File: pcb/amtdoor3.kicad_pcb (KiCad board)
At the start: 2 copper layers, 65 x 30 mm, 45 parts, among them P1 CONN_01X03, P2 dnp-REF-182665-01, P3 CONN_01X03, P4 CONN_01X04, P5 CONN_01X02, P6 CONN_01X02, Q1 Q_NMOS_GSD, Q2 Q_PMOS_HP, Q3 DMMT3906_Dual_PNP, Q4 Q_NMOS_GSD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

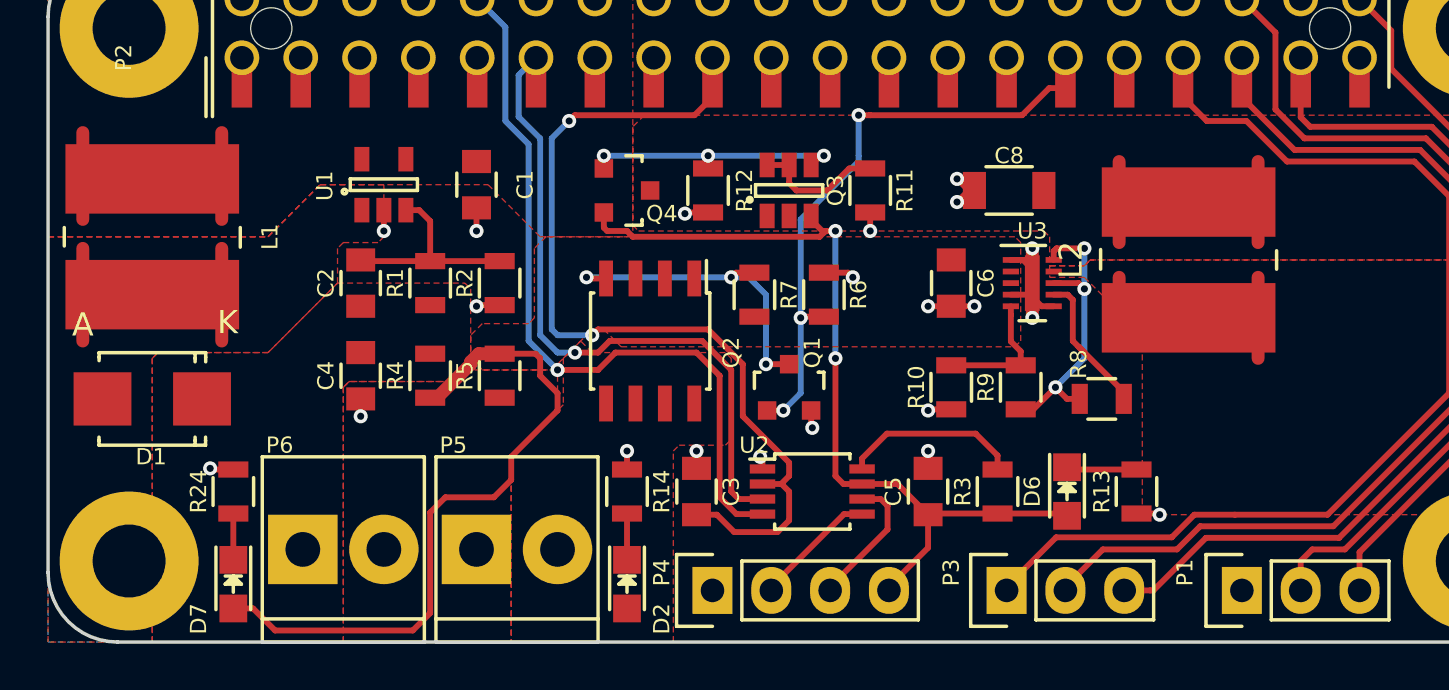
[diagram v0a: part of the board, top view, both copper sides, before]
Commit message: clean up silkscreen, set soldermask expansion, write gerbers
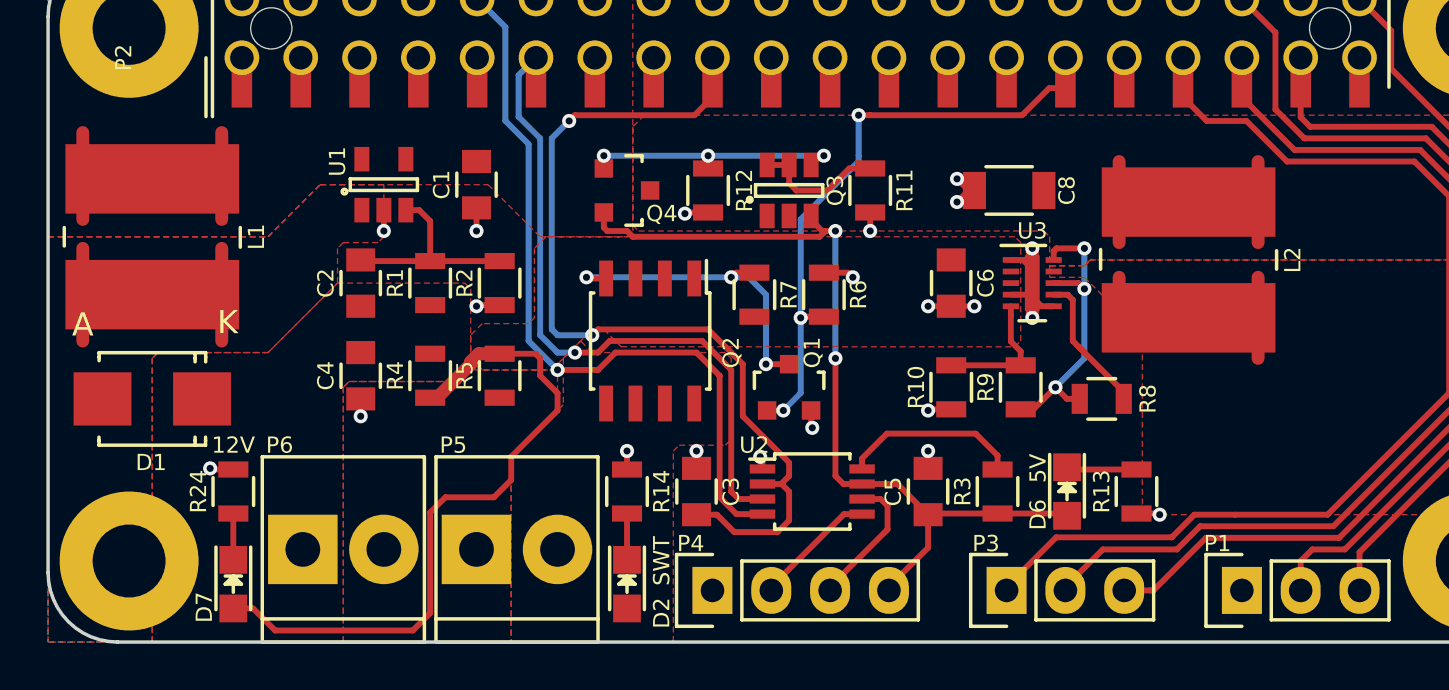
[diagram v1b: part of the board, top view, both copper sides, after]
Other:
- rule pad_to_mask_clearance: 0.2 -> 0.051
- board text added: "12V"
- board text added: "5V"
- board text added: "SWT"
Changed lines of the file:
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@@
     (links 142)
     (no_connects 0)
-    (area 97.2318 83.759999 167.261533 132.2682)
+    (area 97.2318 97.3318 167.261533 132.2682)
     (thickness 1.6)
-    (drawings 16)
+    (drawings 11)
     (tracks 389)
     (zones 0)
@@
     (pad_size 1.524 1.524)
     (pad_drill 0.762)
-    (pad_to_mask_clearance 0.2)
+    (pad_to_mask_clearance 0.051)
+    (solder_mask_min_width 0.077)
     (aux_axis_origin 0 0)
     (visible_elements FFFFFF7F)
     (pcbplotparams
-      (layerselection 0x00030_80000001)
-      (usegerberextensions false)
+      (layerselection 0x010fc_80000001)
+      (usegerberextensions true)
       (excludeedgelayer true)
       (linewidth 0.100000)
@@
       (viasonmask false)
       (mode 1)
-      (useauxorigin false)
+      (useauxorigin true)
       (hpglpennumber 1)
       (hpglpenspeed 20)
@@
       (outputformat 1)
       (mirror false)
-      (drillshape 1)
+      (drillshape 0)
       (scaleselection 1)
-      (outputdirectory ""))
+      (outputdirectory gerber/))
   )
   (net 0 "")
@@
     (tags "Diode SMB Standard")
     (attr smd)
-    (fp_text reference D1 (at 0.05 -2.5 180) (layer F.SilkS)
+    (fp_text reference D1 (at 0.05 -2.75 180) (layer F.SilkS)
       (effects (font (size 0.7 0.7) (thickness 0.15)))
     )
@@
     (tags "Choke, Drossel, WE-PD2, Typ L, Wuerth, SMD,")
     (attr smd)
-    (fp_text reference L1 (at 0 -5.08 270) (layer F.SilkS)
+    (fp_text reference L1 (at 0 -4.5 270) (layer F.SilkS)
       (effects (font (size 0.7 0.7) (thickness 0.15)))
     )
@@
     (descr "Through hole socket strip")
     (tags "socket strip")
-    (fp_text reference P1 (at -2.46 -0.77 90) (layer F.SilkS)
+    (fp_text reference P1 (at -1.05 -2.02 180) (layer F.SilkS)
       (effects (font (size 0.7 0.7) (thickness 0.15)))
     )
@@
     (descr "Through hole socket strip")
     (tags "socket strip")
-    (fp_text reference P3 (at -2.39 -0.77 90) (layer F.SilkS)
+    (fp_text reference P3 (at -0.89 -2.02 180) (layer F.SilkS)
       (effects (font (size 0.7 0.7) (thickness 0.15)))
     )
@@
     (tags SOT-23-5)
     (attr smd)
-    (fp_text reference U1 (at -0.05 -2.55 90) (layer F.SilkS)
+    (fp_text reference U1 (at 1 -2 90) (layer F.SilkS)
       (effects (font (size 0.7 0.7) (thickness 0.15)))
     )
@@
     (tags "capacitor 0805")
     (attr smd)
-    (fp_text reference C1 (at 0 -2.1 270) (layer F.SilkS)
+    (fp_text reference C1 (at 0 1.5 270) (layer F.SilkS)
       (effects (font (size 0.7 0.7) (thickness 0.15)))
     )
@@
     (tags "LED 0805 SMD")
     (attr smd)
-    (fp_text reference D6 (at 0 1.5 270) (layer F.SilkS)
+    (fp_text reference D6 (at 1 1.25 270) (layer F.SilkS)
       (effects (font (size 0.7 0.7) (thickness 0.15)))
     )
@@
     (tags "LED 0805 SMD")
     (attr smd)
-    (fp_text reference D7 (at 1.5 1.5 270) (layer F.SilkS)
+    (fp_text reference D7 (at 1 1.25 450) (layer F.SilkS)
       (effects (font (size 0.7 0.7) (thickness 0.15)))
     )
@@
     (descr "Through hole socket strip")
     (tags "socket strip")
-    (fp_text reference P4 (at -2.19 -0.77 90) (layer F.SilkS)
+    (fp_text reference P4 (at -0.94 -2.02 180) (layer F.SilkS)
       (effects (font (size 0.7 0.7) (thickness 0.15)))
     )
@@
     (tags "capacitor 1206")
     (attr smd)
-    (fp_text reference C8 (at 0 1.5 180) (layer F.SilkS)
+    (fp_text reference C8 (at -2.5 0 270) (layer F.SilkS)
       (effects (font (size 0.7 0.7) (thickness 0.15)))
     )
@@
     (tags "LED 0805 SMD")
     (attr smd)
-    (fp_text reference D2 (at 1.5 -1.5 270) (layer F.SilkS)
+    (fp_text reference D2 (at 1.25 -1.5 270) (layer F.SilkS)
       (effects (font (size 0.7 0.7) (thickness 0.15)))
     )
@@
     (tags "resistor 0805")
     (attr smd)
-    (fp_text reference R8 (at -1 -1.5 90) (layer F.SilkS)
+    (fp_text reference R8 (at 2 0 90) (layer F.SilkS)
       (effects (font (size 0.7 0.7) (thickness 0.15)))
     )
@@
     (tags "Choke, Drossel, WE-PD2, Typ L, Wuerth, SMD,")
     (attr smd)
-    (fp_text reference L2 (at 0 -5.08 90) (layer F.SilkS)
-      (effects (font (size 1 1) (thickness 0.15)))
+    (fp_text reference L2 (at 0 4.5 90) (layer F.SilkS)
+      (effects (font (size 0.7 0.7) (thickness 0.15)))
     )
     (fp_text value 10uH (at 0 6.35 90) (layer F.Fab)
-      (effects (font (size 1 1) (thickness 0.15)))
+      (effects (font (size 0.7 0.7) (thickness 0.15)))
     )
     (fp_line (start -0.39878 3.79984) (end 0.39878 3.79984) (layer F.SilkS) (width 0.15))
@@
       (net 47 /VOS_5V))
   )
-  (gr_line (start 160.06 96.56) (end 142.28 96.56) (layer F.CrtYd) (width 0.2))
-  (gr_line (start 160.06 83.86) (end 160.06 96.56) (layer F.CrtYd) (width 0.2))
-  (gr_line (start 142.28 83.86) (end 160.06 83.86) (layer F.CrtYd) (width 0.2))
-  (gr_line (start 142.28 96.56) (end 142.28 83.86) (layer F.CrtYd) (width 0.2))
-  (gr_line (start 138.24 84.4) (end 138.24 94.56) (layer F.CrtYd) (width 0.2))
-  (gr_line (start 125.54 84.4) (end 138.24 84.4) (layer F.CrtYd) (width 0.2))
-  (gr_line (start 125.54 94.56) (end 125.54 84.4) (layer F.CrtYd) (width 0.2))
-  (gr_line (start 138.24 94.56) (end 125.54 94.56) (layer F.CrtYd) (width 0.2))
+  (gr_text 12V (at 108 121.5) (layer F.SilkS)
+    (effects (font (size 0.7 0.7) (thickness 0.15)))
+  )
+  (gr_text SWT (at 126.5 126.5 90) (layer F.SilkS)
+    (effects (font (size 0.7 0.7) (thickness 0.15)))
+  )
+  (gr_text 5V (at 142.75 122.5 90) (layer F.SilkS)
+    (effects (font (size 0.7 0.7) (thickness 0.15)))
+  )
   (gr_arc (start 162 127) (end 165 127) (angle 90) (layer Edge.Cuts) (width 0.15))
   (gr_arc (start 162 103) (end 162 100) (angle 90) (layer Edge.Cuts) (width 0.15))

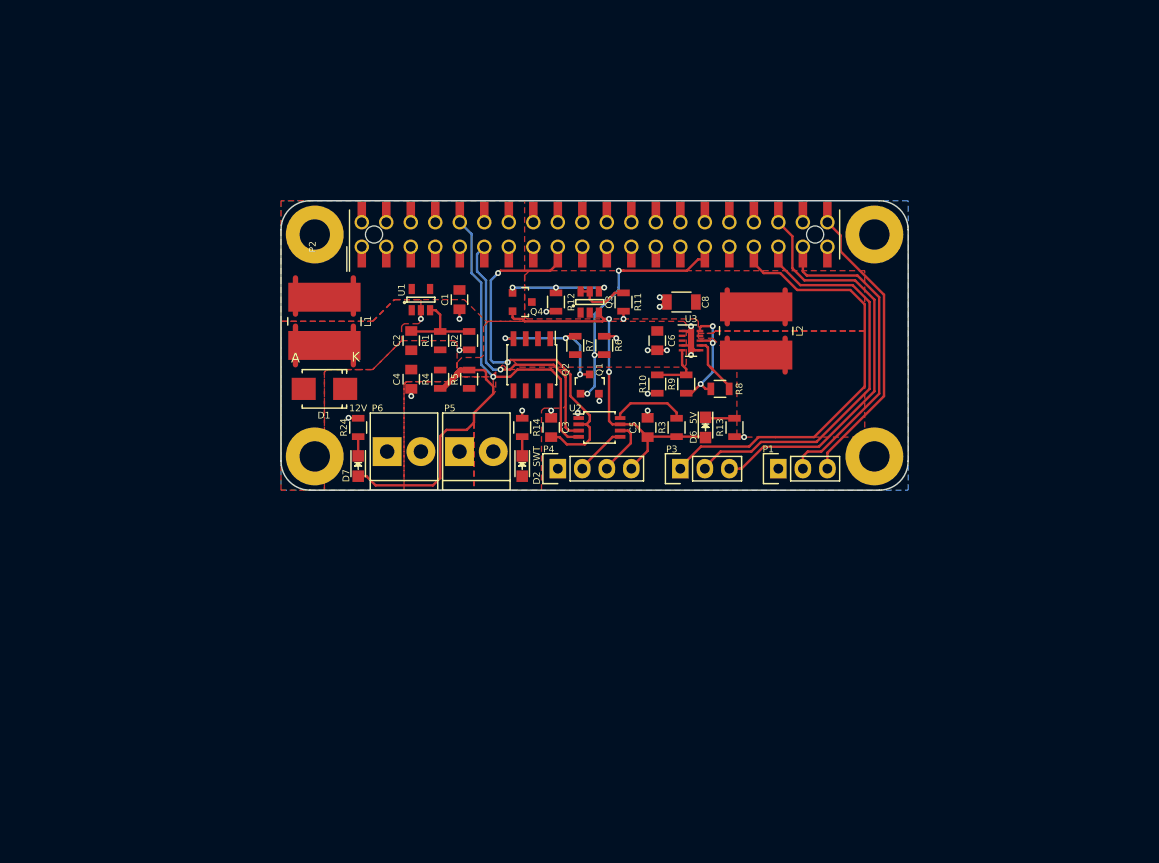
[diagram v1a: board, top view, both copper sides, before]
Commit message: new rev schematic updates and footprint grouping
* change level shifter to NFET gates w/ pull up b/c NVT2002 leaks 5V EN to 3.3V rail
* add selectable, fused output voltage to each port
* rename P2 to P4 so the output ports are P1, P2, P3
* use level shifting on all ports
* reassign GPIO to ports so we have UART TX+RX, PWM, and plain GPIO
* add fuses and DNPs so boost and buck can be populated but not interfere
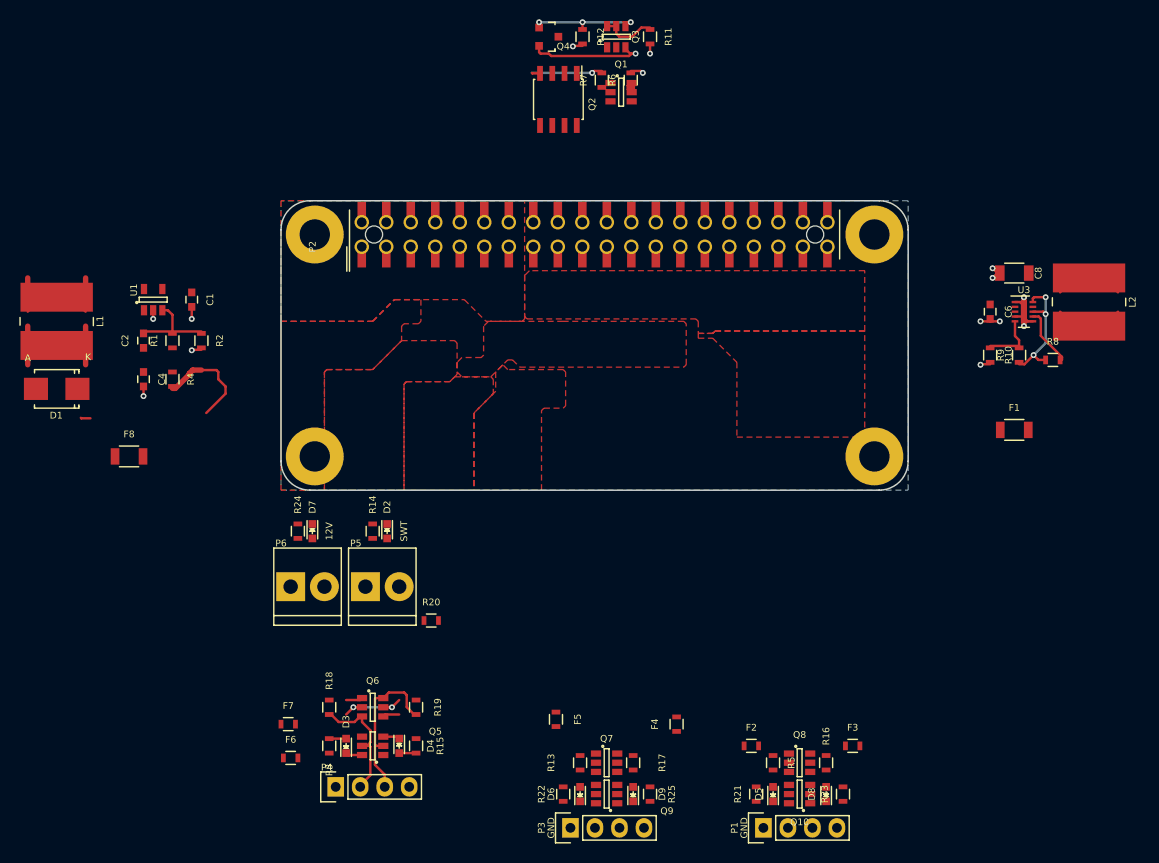
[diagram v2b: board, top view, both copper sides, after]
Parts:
- removed C3, C5: 0.1uF, Capacitors_SMD:C_0805
- removed U2: NVT2002, Housings_SSOP:TSSOP-8_3x3mm_Pitch0.65mm
- added D3: LED Green, LEDs:LED_0603, F.Cu at (106.8, 156.5)
- added D4: LED Green, LEDs:LED_0603, F.Cu at (112.2, 156.5)
- added D5: LED Green, LEDs:LED_0603, F.Cu at (151.0, 161.5)
- added D8: LED Green, LEDs:LED_0603, F.Cu at (156.5, 161.5)
- added D9: LED Green, LEDs:LED_0603, F.Cu at (136.5, 161.5)
- added F1: 250mA, Resistors_SMD:R_1206, F.Cu at (176.0, 123.8)
- added F2: F_Small, Resistors_SMD:R_0603, F.Cu at (148.8, 156.5)
- added F3: F_Small, Resistors_SMD:R_0603, F.Cu at (159.2, 156.5)
- added F4: F_Small, Resistors_SMD:R_0603, F.Cu at (141.0, 154.2)
- added F5: F_Small, Resistors_SMD:R_0603, F.Cu at (128.5, 153.8)
- added F6: F_Small, Resistors_SMD:R_0603, F.Cu at (101.0, 157.8)
- added F7: F_Small, Resistors_SMD:R_0603, F.Cu at (100.8, 154.2)
- added F8: 500mA, Resistors_SMD:R_1206, F.Cu at (84.2, 126.5)
- added Q10: Q_NMOS_DUAL, TO_SOT_Packages_SMD:SOT-23-6, F.Cu at (153.8, 161.5)
- added Q5: Q_NMOS_DUAL, TO_SOT_Packages_SMD:SOT-23-6, F.Cu at (109.5, 156.5)
- added Q6: Q_NMOS_DUAL, TO_SOT_Packages_SMD:SOT-23-6, F.Cu at (109.5, 152.5)
- added Q7: Q_NMOS_DUAL, TO_SOT_Packages_SMD:SOT-23-6, F.Cu at (133.8, 158.2)
- added Q8: Q_NMOS_DUAL, TO_SOT_Packages_SMD:SOT-23-6, F.Cu at (153.8, 158.2)
- added Q9: Q_NMOS_DUAL, TO_SOT_Packages_SMD:SOT-23-6, F.Cu at (133.8, 161.5)
- added R15: 1k, Resistors_SMD:R_0603, F.Cu at (114.0, 156.5)
- added R16: 10k, Resistors_SMD:R_0603, F.Cu at (156.5, 158.2)
- added R17: 10k, Resistors_SMD:R_0603, F.Cu at (136.5, 158.2)
- added R18: 10k, Resistors_SMD:R_0603, F.Cu at (105.0, 152.5)
- added R19: 10k, Resistors_SMD:R_0603, F.Cu at (114.0, 152.5)
- added R20: 10k, Resistors_SMD:R_0603, F.Cu at (115.6, 143.5)
- added R21: 1k, Resistors_SMD:R_0603, F.Cu at (149.2, 161.5)
- added R22: 1k, Resistors_SMD:R_0603, F.Cu at (129.2, 161.5)
- added R23: 1k, Resistors_SMD:R_0603, F.Cu at (158.2, 161.5)
- added R25: 1k, Resistors_SMD:R_0603, F.Cu at (138.2, 161.5)
- C1, C2, C6: footprint Capacitors_SMD:C_0805 -> Capacitors_SMD:C_0603
- C4: value 4.7uF -> 4.7uF 25V; footprint Capacitors_SMD:C_0805 -> Capacitors_SMD:C_0603
- C8: value 22uF -> 22uF 10V
- D1: value 10BQ015 -> 15V 1A
- D2, D6, D7: footprint LEDs:LED_0805 -> LEDs:LED_0603
- P1, P3: value CONN_01X03 -> CONN_01X04; footprint Socket_Strips:Socket_Strip_Straight_1x03 -> Socket_Strips:Socket_Strip_Straight_1x04
- Q1: value Q_NMOS_GSD -> Q_NMOS_DUAL; footprint TO_SOT_Packages_SMD:SOT-23 -> TO_SOT_Packages_SMD:SOT-23-6
- Q4: value Q_NMOS_GSD -> Q_PMOS_GSD
- R1, R10, R11, R12, R14, R2, R24, R4, R6, R7, R8, R9: footprint Resistors_SMD:R_0805 -> Resistors_SMD:R_0603
- R13: value 1k -> 10k; footprint Resistors_SMD:R_0805 -> Resistors_SMD:R_0603
- R3: value 10k -> 1k; footprint Resistors_SMD:R_0805 -> Resistors_SMD:R_0603
- R5: value dnp -> 10k; footprint Resistors_SMD:R_0805 -> Resistors_SMD:R_0603
- moved R5 50.7 mm to (151.0, 158.2)
- moved R3 48.8 mm to (105.0, 156.5)
- moved P4 40.2 mm to (105.7, 160.8)
- moved D6 40.2 mm to (131.0, 161.5), turned to 90 degrees
- moved P3 38.9 mm to (130.0, 165.0)
- moved R13 38.3 mm to (131.0, 158.2)
- moved P1 37.3 mm to (150.0, 165.0)
- moved C6 34.6 mm to (173.5, 111.5)
- moved C8 34.6 mm to (176.0, 107.5)
- moved L2 34.6 mm to (183.8, 110.5)
- moved R10 34.6 mm to (173.5, 116.0)
- moved R8 34.6 mm to (180.0, 116.5)
- moved R9 34.6 mm to (176.5, 116.0)
- moved U3 34.6 mm to (177.0, 111.5)
- moved Q1 30.4 mm to (135.2, 88.8)
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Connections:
- net /FB_12V renamed /BST_FB
- net /SW_12V renamed /BST_SW
- net /VSWITCHED_T renamed /P12V_SW
- C1 pad 1: +5V -> /P5V_BST
- C2 pad 1: +12V -> Net-(C2-Pad1)
- C4 pad 1: +12V -> Net-(C2-Pad1)
- C6 pad 1: /VSWITCHED -> Net-(C6-Pad1)
- D1 pad 1: +12V -> Net-(C2-Pad1)
- D6 pad 2: +5V -> Net-(D6-Pad2)
- D7 pad 2: /VSWITCHED -> +12V
- H1 pad 1: Net-(H1-Pad1) -> (no net)
- H2 pad 1: Net-(H2-Pad1) -> (no net)
- H3 pad 1: Net-(H3-Pad1) -> (no net)
- H4 pad 1: Net-(H4-Pad1) -> (no net)
- L1 pad 1: +5V -> /P5V_BST
- P1 pad 1: /GPIO20 -> GND
- P1 pad 2: /GPIO26 -> /PORT3-1
- P1 pad 3: /GPIO21_SCLK -> /PORT3-2
- P2 pad 17: +3V3 -> /RPI_3V3_2
- P3 pad 1: /GPIO13 -> GND
- P3 pad 2: /GPIO19 -> /PORT2-1
- P3 pad 3: /GPIO16_CE2# -> /PORT2-2
- P4 pad 4: +5V -> /VPORT1
- P6 pad 2: /VAUX -> +12V
- Q1 pad 1: /GPIO5 -> GND
- Q1 pad 2: GND -> /GPIO5
- Q1 pad 3: /VSW_D -> /GPIO22
- Q2 pad 1: /VSWITCHED -> +12V
- Q2 pad 2: /VSWITCHED -> +12V
- Q2 pad 3: /VSWITCHED -> +12V
- Q2 pad 4: /VSW_D -> /SW_D
- R1 pad 1: +12V -> Net-(C2-Pad1)
- R13 pad 1: Net-(D6-Pad1) -> /VPORT2
- R13 pad 2: GND -> /PORT2-1
- R3 pad 1: +5V -> /VPORT1
- R4 pad 1: +12V -> /P5V_BST
- R4 pad 2: /VSWITCHED -> +5V
- R5 pad 1: /VSWITCHED -> /VPORT3
- R5 pad 2: /VAUX -> /PORT3-1
- R7 pad 1: /VSWITCHED -> +12V
- R7 pad 2: /VSW_D -> /SW_D
- U1 pad 4: +5V -> /P5V_BST
- U1 pad 5: +5V -> /P5V_BST
- U3 pad 2: /VSWITCHED -> Net-(C6-Pad1)
- U3 pad 3: /VSWITCHED -> Net-(C6-Pad1)
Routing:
- net /GPIO13: track 46.2 -> 1.71 mm
- net /GPIO16_CE2#: track 44.4 -> 1.31 mm
- net /GPIO19: track 42.4 -> 1.71 mm
- net +3V3: track 39.9 -> 0.00 mm, vias 2 -> 0
- net +5V: track 56.3 -> 17.4 mm, vias 2 -> 1
- net /GPIO26: track 33.5 -> 1.31 mm
- net /GPIO15_RXD0: track 33.9 -> 3.04 mm, vias 1 -> 0
- net /GPIO21_SCLK: track 31.7 -> 1.31 mm
- net /VSWITCHED: track 29.7 -> 0.00 mm
- net /GPIO17: track 30.0 -> 1.31 mm, vias 1 -> 0
- net /GPIO5: track 26.5 -> 1.31 mm, vias 3 -> 0
- net /P5V_BST: track 0.00 -> 15.5 mm
- net /VSW_D: track 14.0 -> 0.00 mm, vias 3 -> 0
- net /RFID_EN: track 5.90 -> 16.7 mm
- net /VPORT3: track 0.00 -> 9.19 mm
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- added copper zone on F.Cu, net /SW_12V
- added copper zone on F.Cu, net /VSWITCHED_T
- removed copper zone on F.Cu, net /BST_SW
- removed copper zone on F.Cu, net /P12V_SW
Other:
- board text added: "GND"
- board text removed: "5V"
